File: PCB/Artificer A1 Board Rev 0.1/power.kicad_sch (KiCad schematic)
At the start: 15 parts, among them U12 AXP323, U2 AXP717, U5 CH217K, U6 GT-USB-7010ASV

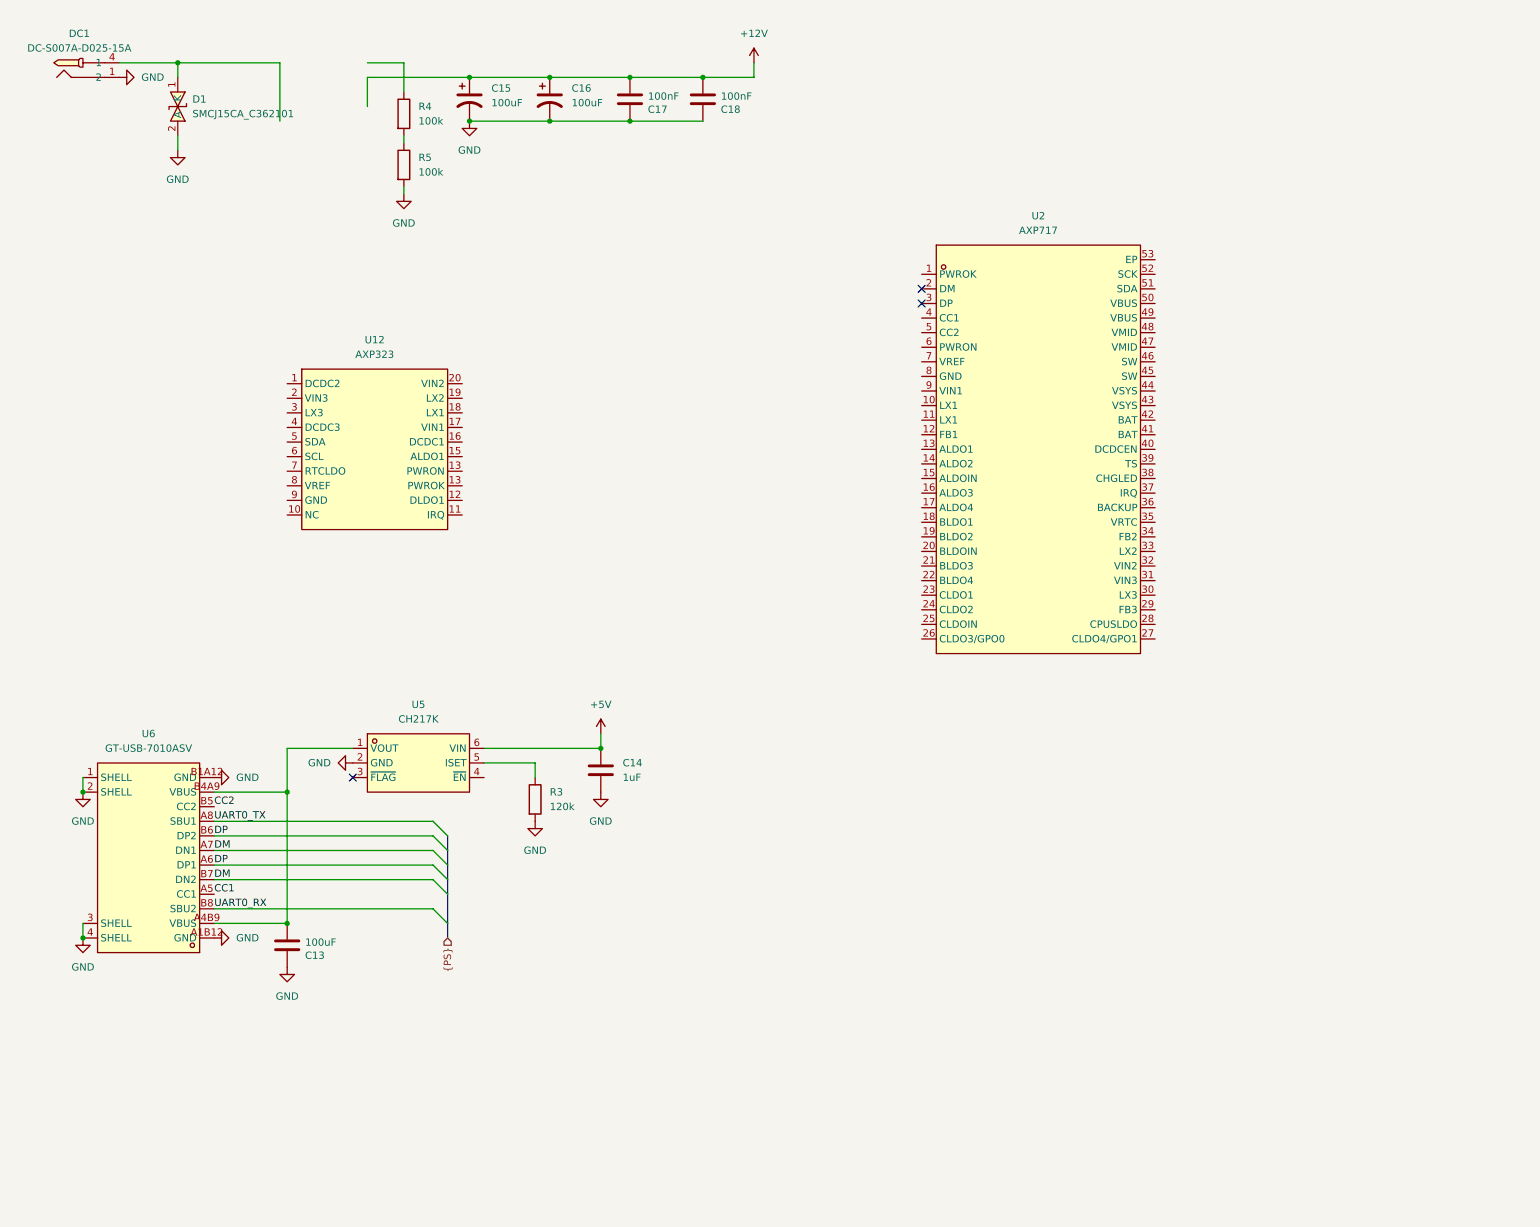
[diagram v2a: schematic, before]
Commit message: dc-dc & started eth PHY
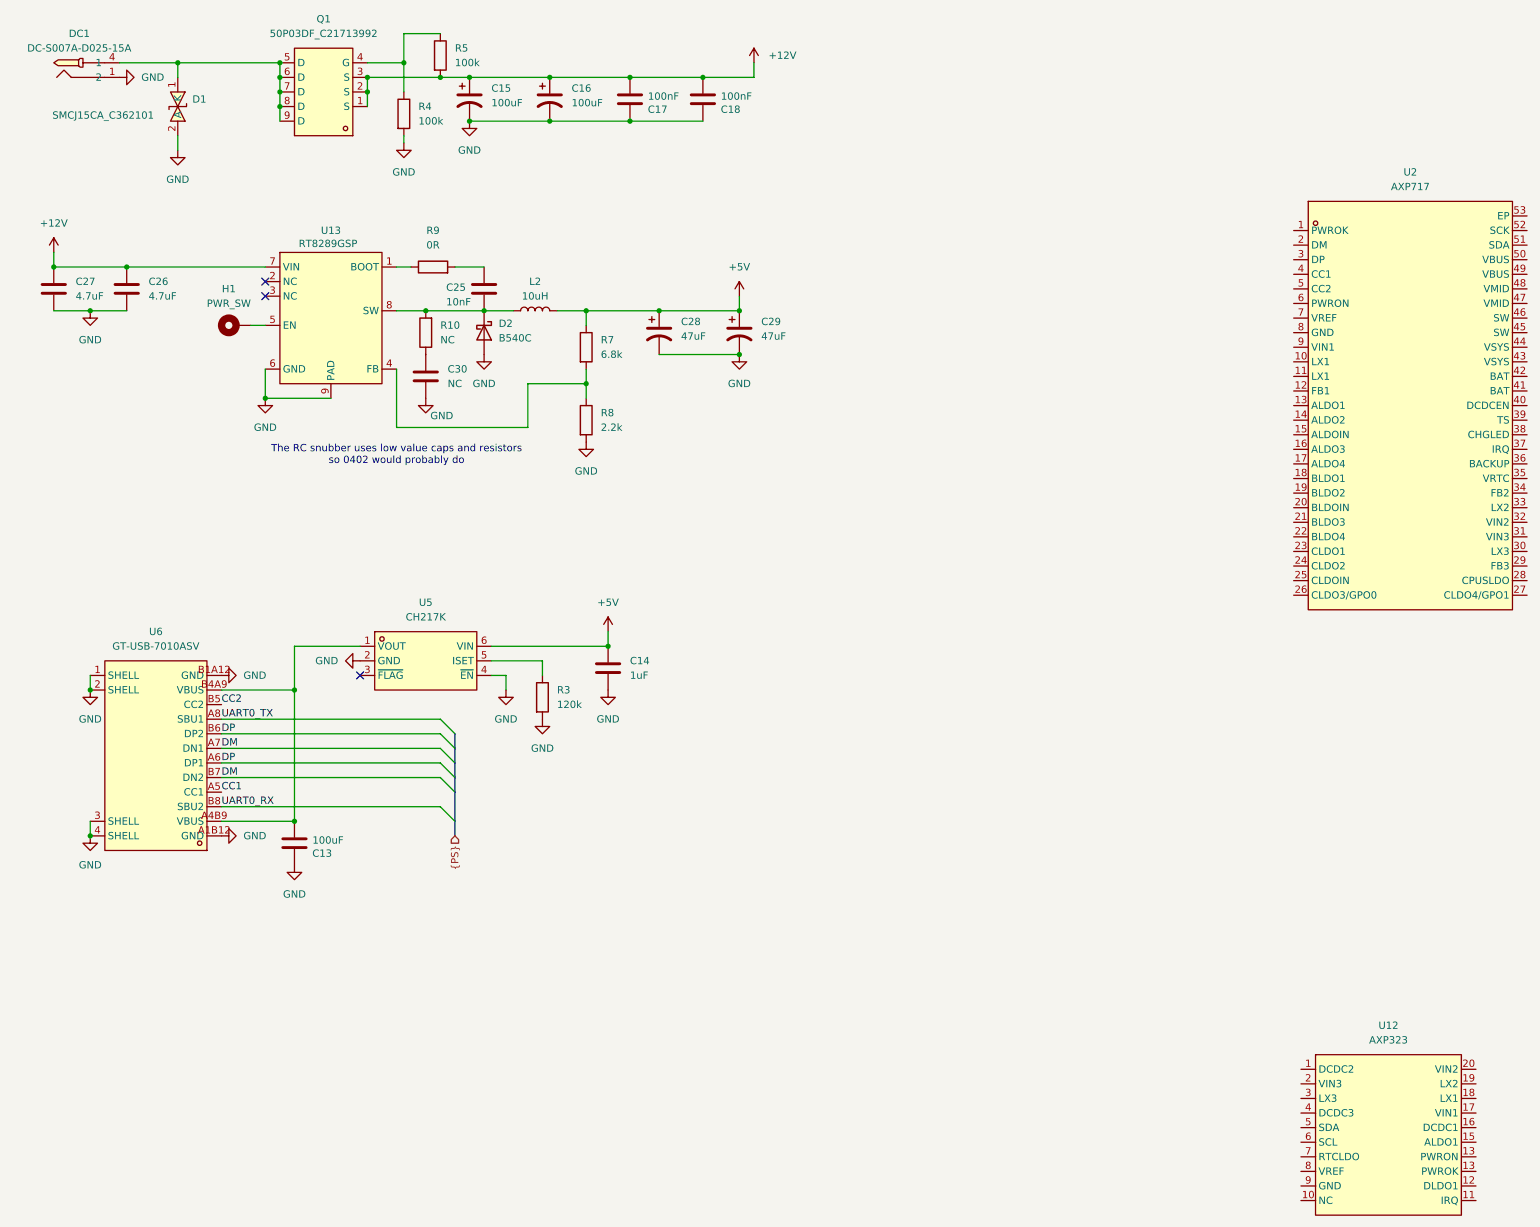
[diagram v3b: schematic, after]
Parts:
- added C25: 10nF, symbol Device:C
- added C26, C27: 4.7uF, symbol Device:C
- added C28, C29: 47uF, symbol Device:C_Polarized_US
- added C30: NC, symbol Device:C
- added D2: B540C, Diode_SMD:D_SMC, symbol Device:D_Schottky
- added H1: PWR_SW, symbol Mechanical:MountingHole_Pad_MP
- added L2: 10uH, symbol Device:L
- added Q1: 50P03DF_C21713992, easyeda:PDFN-8_L3.2-W3.0-P0.65-LS3.3-BL-1, symbol easyeda:30P03D_C20754801
- added R10: NC, symbol Device:R
- added R7: 6.8k, symbol Device:R
- added R8: 2.2k, symbol Device:R
- added R9: 0R, symbol Device:R
- added U13: RT8289GSP, easyeda:SOIC-8_L5.0-W4.0-P1.27-LS6.0-BL-EP2.0, symbol easyeda:RT8289GSP
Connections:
- net +12V: now also R5.2, C26.2, C27.2, Q1.1 (S), Q1.2 (S), Q1.3 (S), U13.7 (VIN)
- net +5V: now also C28.1, C29.1, L2.2, R7.1
- net GND: now also R4.2, U5.4 (~{EN}), C26.1, C27.1, C28.2, C29.2, C30.2, D2.2 (A), R8.2, U13.6 (GND), U13.9 (PAD); no longer R5.2
- net at R5.1: now also R4.1, Q1.4 (G); no longer R4.2
- net at D1.1 (K), DC1.4 (1): now also Q1.5 (D), Q1.6 (D), Q1.7 (D), Q1.8 (D), Q1.9 (D)
- new net: C25.1, D2.1 (K), L2.1, R10.2, U13.8 (SW)
- new net: R9.1, U13.1 (BOOT)
- new net: R7.2, R8.1, U13.4 (FB)
- new net: H1.MP, U13.5 (EN)
- new net: C25.2, R9.2
- new net: C30.1, R10.1
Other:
- note added: "The RC snubber uses low value caps and resistors so 0402 would probably do"
- moved on the sheet: C13, C14, R3, R5, U12, U2, U5, U6

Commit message: added a few accessories
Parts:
- removed C13: 100uF, symbol Device:C
- removed C14: 1uF, symbol Device:C
- removed R3: 120k, symbol Device:R
- removed U5: CH217K, easyeda:SOT-23-6_L2.9-W1.6-P0.95-LS2.8-BL, symbol easyeda:CH217K
- removed U6: GT-USB-7010ASV, easyeda:USB-C-SMD_G-SWITCH_GT-USB-7010ASV, symbol easyeda:GT-USB-7010ASV
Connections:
- no-connect marks 3 -> 2

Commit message: added: sd, wifi, audio, started power, fixed buses
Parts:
- removed H1: PWR_SW, symbol Mechanical:MountingHole_Pad_MP
- removed U12: AXP323, custom footprints:AXP323, symbol AXP323:AXP323
- removed U2: AXP717, easyeda:QFN-52_L6.0-W6.0-P0.40-TL-EP4.7, symbol easyeda:AXP717
- added C100, C101, C102, C103, C104, C105, C106, C107, C87, C95, C96, C97, C98: 2.2uF, symbol Device:C_Small
- added C108, C81, C83, C84, C88, C92, C93, C94, C99: 1uF, symbol Device:C_Small
- added C79, C80: 1nF, symbol Device:C_Small
- added C82, C85, C86, C89, C90, C91: 22uF, symbol Device:C_Small
- added L6, L7, L8: 1uH, symbol Device:L_Small
- added TP10, TP11, TP12, TP13, TP14, TP15, TP16, TP17, TP18, TP19, TP20, TP7, TP9: CPUSLDO, symbol Connector:TestPoint
- added TP3: PWR_SW, symbol Connector:TestPoint
- added TP4: DCDC1, symbol Connector:TestPoint
- added TP5: DCDC2, symbol Connector:TestPoint
- added TP6: DCDC3, symbol Connector:TestPoint
- added TP8: VCC-RTC, symbol Connector:TestPoint
- added U1: T527M00X0DCH, easyeda:BGA-664_L17.0-W17.0_T527, symbol easyeda:T527M00X0DCH
- added U2: AXP323, custom footprints:AXP323, symbol AXP323:AXP323
- added U4: AXP717B, easyeda:QFN-52_L6.0-W6.0-P0.40-TL-EP4.5, symbol easyeda:AXP717B
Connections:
- net +5V: now also C108.1, C81.1, C83.1, C84.1, C94.1, C99.1, U4.15 (ALDOIN), U4.20 (BLDOIN), U4.25 (CLDOIN), U4.31 (VIN3), U4.32 (VIN2), U4.9 (VIN1)
- net GND: now also C100.2, C101.2, C102.2, C103.2, C104.2, C105.2, C106.2, C107.2, C108.2, C79.2, C80.2, C81.2, C82.2, C83.2, C84.2, C85.2, C86.2, C87.2, C88.2, C89.2, C90.2, C91.2, C92.2, C93.2, C94.2, C95.2, C96.2, C97.2, C98.2, C99.2, U1.A1 (GND), U1.A32 (AVSS), U1.A33 (AVSS), U1.AA15 (GND), U1.AA16 (GND), U1.AA18 (GND), U1.AA21 (GND), U1.AA22 (GND), U1.AA26 (GND), U1.AA30 (GND), U1.AA32 (GND), U1.AB10 (GND), U1.AB11 (GND), U1.AB12 (GND), U1.AB14 (GND), U1.AB15 (GND), U1.AB17 (GND), U1.AC1 (GND), U1.AC26 (GND), U1.AC29 (GND), U1.AC33 (GND), U1.AD11 (GND), U1.AD13 (GND), U1.AD14 (GND), U1.AD20 (GND), U1.AD21 (GND), U1.AD22 (GND), U1.AD9 (GND), U1.AE12 (GND), U1.AE14 (GND), U1.AE18 (GND), U1.AE19 (GND), U1.AE20 (GND), U1.AE21 (GND), U1.AE22 (GND), U1.AE23 (GND), U1.AE24 (GND), U1.AE25 (GND), U1.AE26 (GND), U1.AE29 (GND), U1.AE32 (GND), U1.AE9 (GND), U1.AG11 (GND), U1.AG25 (GND), U1.AG28 (GND), U1.AG3 (GND), U1.AG31 (GND), U1.AG33 (GND), U1.AG6 (GND), U1.AG7 (GND), U1.AH27 (GND), U1.AH32 (GND), U1.AH7 (GND), U1.AH9 (GND), U1.AJ13 (GND), U1.AJ19 (GND), U1.AJ21 (GND), U1.AJ23 (GND), U1.AK11 (GND), U1.AK32 (GND), U1.AK5 (GND), U1.AL12 (GND), U1.AL13 (GND), U1.AL14 (GND), U1.AL3 (GND), U1.AL9 (GND), U1.AM20 (GND), U1.AM26 (GND), U1.AM29 (GND), U1.AM5 (GND), U1.AN1 (GND), U1.AN10 (GND), U1.AN11 (GND), U1.AN18 (GND), U1.AN22 (GND), U1.AN24 (GND), U1.AN28 (GND), U1.AN31 (GND), U1.AN33 (GND), U1.C10 (GND), U1.C12 (GND), U1.C14 (GND), U1.C18 (GND), U1.C20 (GND), U1.C22 (AVSS), U1.C24 (AVSS), U1.C26 (AVSS), U1.C28 (AVSS), U1.C30 (AVSS), U1.C31 (AVSS), U1.C6 (GND), U1.C8 (GND), U1.D6 (GND), U1.E29 (AVSS), U1.E3 (GND), U1.F10 (GND), U1.F12 (GND), U1.F22 (AVSS), U1.F24 (AVSS), U1.F6 (GND), U1.F8 (GND), U1.G10 (GND), U1.G14 (GND), U1.G18 (GND), U1.G26 (AVSS), U1.G28 (AVSS), U1.G29 (GND), U1.G3 (GND), U1.G8 (GND), U1.H24 (AVSS), U1.J10 (GND), U1.J12 (GND), U1.J13 (GND), U1.J17 (AVSS), U1.J21 (AVSS), U1.J22 (AVSS), U1.J23 (AVSS), U1.J26 (AVSS), U1.J28 (GND), U1.J3 (GND), U1.J31 (GND), U1.J6 (GND), U1.J9 (GND), U1.K10 (GND), U1.K11 (GND), U1.K12 (GND), U1.K15 (AVSS), U1.K16 (AVSS), U1.K21 (AVSS), U1.K22 (AVSS), U1.K24 (AVSS), U1.K25 (AVSS), U1.K26 (GND), U1.K9 (GND), U1.L10 (GND), U1.L12 (GND), U1.L13 (GND), U1.L16 (AVSS), U1.L19 (AVSS), U1.L24 (AVSS), U1.L27 (GND), U1.L3 (GND), U1.L30 (GND), U1.L33 (GND), U1.L6 (GND), U1.M13 (GND), U1.M16 (AVSS), U1.M18 (AVSS), U1.M19 (AVSS), U1.N10 (GND), U1.N12 (GND), U1.N15 (GND), U1.N18 (GND), U1.N19 (GND), U1.N22 (GND), U1.N26 (GND), U1.N27 (GND), U1.N3 (GND), U1.N30 (GND), U1.N6 (GND), U1.P11 (GND), U1.P16 (GND), U1.P19 (GND), U1.P24 (GND), U1.R11 (GND), U1.R13 (GND), U1.R19 (GND), U1.R24 (GND), U1.R27 (GND), U1.R3 (GND), U1.R7 (GND), U1.T15 (GND), U1.T16 (GND), U1.T18 (GND), U1.T24 (GND), U1.U14 (GND), U1.U16 (GND), U1.U25 (GND), U1.U27 (GND), U1.U7 (GND), U1.V18 (GND), U1.V19 (GND), U1.W12 (GND), U1.W13 (GND), U1.W15 (GND), U1.W16 (GND), U1.W22 (GND), U1.W27 (GND), U1.W30 (GND), U1.Y15 (GND), U1.Y18 (GND), U1.Y22 (GND), U1.Y23 (GND), U1.Y26 (GND), U2.21 (EPAD), U2.9 (GND), U4.53 (EP), U4.8 (GND)
- net at U13.5 (EN): now also TP3.1
- new net: L6.1, U4.10 (LX1_1), U4.11 (LX1_2)
- new net: L8.1, U4.30 (LX3)
- new net: L7.1, U4.33 (LX2)
- new net: C88.1, U4.7 (VREF)
- new net: U1.AA12 (VDDDNR), U1.AA13 (VDDDNR), U1.Y12 (VDDDNR), U1.Y13 (VDDDNR)
- new net: U1.N21 (VDDDE), U1.P21 (VDDDE)
- new net: U1.T11 (VDDGPU), U1.T13 (VDDGPU), U1.U12 (VDDGPU), U1.U13 (VDDGPU)
- new net: U1.T19 (VDDCPUB), U1.T21 (VDDCPUB), U1.T22 (VDDCPUB), U1.U18 (VDDCPUB), U1.U19 (VDDCPUB), U1.U21 (VDDCPUB), U1.U22 (VDDCPUB)
- new net: U1.W19 (VDDCPUL), U1.W21 (VDDCPUL), U1.Y19 (VDDCPUL), U1.Y21 (VDDCPUL)
- new net ALDO1: C104.1, TP17.1, U4.13 (ALDO1)
- new net ALDO2: C105.1, TP18.1, U4.14 (ALDO2)
- new net ALDO3: C106.1, TP19.1, U4.16 (ALDO3)
- new net ALDO4: C107.1, TP20.1, U4.17 (ALDO4)
- new net AP-NMI: C79.1, U4.37 (IRQ)
- new net AP-RESET: C80.1, U4.1 (PWROK)
- new net BLDO1: C100.1, TP16.1, U4.18 (BLDO1)
- new net BLDO2: C101.1, TP15.1, U4.19 (BLDO2)
- new net BLDO3: C102.1, TP14.1, U4.21 (BLDO3)
- new net BLDO4: C103.1, TP13.1, U4.22 (BLDO4)
- new net CLDO1: C95.1, TP9.1, U4.23 (CLDO1)
- new net CLDO2: C96.1, TP10.1, U4.24 (CLDO2)
- new net CLDO3: C97.1, TP11.1, U4.26 (CLDO3/GPO0)
- new net CLDO4: C98.1, TP12.1, U4.27 (CLDO4/GPO1)
- new net CPUSLDO: C87.1, TP7.1, U4.28 (CPUSLDO)
- new net DCDC1: C82.1, C89.1, L6.2, TP4.1
- new net DCDC2: C85.1, C90.1, L7.2, TP5.1
- new net DCDC3: C86.1, C91.1, L8.2, TP6.1, U4.29 (FB3)
- new net PMU-SCK: U4.52 (SCK)
- new net PMU-SDA: U4.51 (SDA)
- new net VCC-RTC: C92.1, TP8.1, U4.35 (VRTC)
- new net VCC-RTC-IN: C93.1, U4.36 (BACKUP)
- new net VDD06-DRAM: U1.AC17 (VCCDRAML), U1.AC18 (VCCDRAML), U1.AC19 (VCCDRAML), U1.AC20 (VCCDRAML), U1.AC22 (VCCDRAML)
- new net VDD11-DRAM: U1.AA24 (VCCDRAM), U1.AB24 (VCCDRAM), U1.AC24 (VCCDRAM), U1.W23 (VCCDRAM), U1.W24 (VCCDRAM), U1.W25 (VCCDRAM), U1.Y24 (VCCDRAM)
- new net VDD18-DRAM: U1.AD25 (VDD18-DRAM)
- no-connect marks 2 -> 8
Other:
- note added: "VDD-CPULFB"
- note added: "VDD-SYSFB"

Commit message: added features
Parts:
- added C109, C110, C111, C113: 22uF, symbol Device:C_Small
- added C112, C118, C119, C120: 4.7uF, symbol Device:C_Small
- added C114, C115, C116, C117, C121, C122, C124, C125, C126, C127: 10uF, symbol Device:C_Small
- added C123: 100nF, symbol Device:C_Small
- added C128: 1uF, symbol Device:C_Small
- added C129, C130, C131: 2.2uF, symbol Device:C_Small
- added C132, C133: 4.7uF, symbol Device:C
- added C134: NC, symbol Device:C
- added C135: 10nF, symbol Device:C
- added C136, C137: 47uF, symbol Device:C_Polarized_US
- added D13: B540C, Diode_SMD:D_SMC, symbol Device:D_Schottky
- added D14, D15: SS54, Diode_SMD:D_SMA, symbol Device:D_Schottky
- added L10, L11, L12, L9: 1uH, symbol Device:L_Small
- added L13: 10uH, symbol Device:L
- added NT1, NT10, NT11, NT12, NT13, NT14, NT15, NT16, NT17, NT18, NT19, NT2, NT20, NT21, NT22, NT23, NT24, NT25, NT26, NT27, NT28, NT29, NT3, NT30, NT31, NT32, NT33, NT34, NT35, NT36, NT37, NT38, NT39, NT4, NT40, NT41, NT42, NT43, NT44, NT45, NT46, NT47, NT48, NT49, NT5, NT50, NT51, NT52, NT53, NT54, NT6, NT7, NT8, NT9: NetTie_2, symbol Device:NetTie_2
- added PS: CPUSLDO, symbol Connector:TestPoint
- added R77, R80: 0R, symbol Device:R_Small
- added R78: NC, symbol Device:R_Small
- added R79: 10k, symbol Device:R_Small
- added R81: NC, symbol Device:R
- added R82: 0R, symbol Device:R
- added R83: 56k, symbol Device:R
- added R84: 33k, symbol Device:R
- added TP21, TP22: DCDC1, symbol Connector:TestPoint
- added TP23: 3V3_PCIE_PWR_SW, symbol Connector:TestPoint
- added U15: RT8289GSP, easyeda:SOIC-8_L5.0-W4.0-P1.27-LS6.0-BL-EP2.0, symbol easyeda:RT8289GSP
- added U16: ETA8121S2G, easyeda:SOT-23-6_L2.9-W1.6-P0.95-LS2.9-BL, symbol easyeda:ETA8121S2G
- Q1: LCSC Part C21713992 -> C20754801
- R7: value 6.8k -> 68k
- R8: value 2.2k -> 22k
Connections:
- net +12V: now also C132.2, C133.2, U15.7 (VIN)
- net +5V: no longer C28.1, C29.1, L2.2, R7.1
- net ALDO1: now also NT12.1
- net ALDO2: now also NT13.1
- net ALDO3: now also NT14.1, NT15.1
- net ALDO4: now also NT16.1, NT17.1, NT18.1, NT19.1, NT20.1
- net AP-RESET: now also R80.1
- net BLDO1: now also NT21.1, NT22.1
- net BLDO2: now also C123.1, NT23.1, NT24.1, R79.1
- net BLDO3: now also NT25.1
- net BLDO4: now also NT26.1
- net CLDO1: now also NT28.1, NT29.1, NT30.1, NT31.1, NT32.1, NT33.1, NT34.1, NT35.1, NT36.1, NT37.1, NT38.1
- net CLDO2: now also NT27.1
- net CLDO3: now also NT43.1
- net CLDO4: now also NT40.1, NT41.1
- net CPUSLDO: now also NT1.1
- net DCDC1: now also NT3.1
- net DCDC2: now also NT10.1, NT2.1, NT4.1, NT5.1, NT6.1, NT7.1, NT8.1, NT9.1
- net DCDC3: now also NT11.1
- net GND: now also C109.2, C110.2, C111.2, C112.1, C113.2, C114.2, C115.2, C116.2, C117.2, C118.1, C119.1, C120.1, C121.2, C122.2, C123.2, C124.2, C125.2, C126.2, C127.2, C128.1, C129.2, C130.2, C131.2, C132.1, C133.1, C134.2, C136.2, C137.2, D13.2 (A), R78.1, R84.2, U15.6 (GND), U15.9 (PAD)
- net PMU-SCK: now also U2.5 (SDA), TP21.1
- net PMU-SDA: now also U2.6 (SCL), TP22.1
- net VDD18-DRAM: now also NT18.2; no longer U1.AD25 (VDD18-DRAM)
- net 323-DLDO1: now reaches U2.12 (DLDO1)
- net 323-DLDO1: now also C130.1
- net at U2.13 (PWROK): now also R80.2
- net at U2.14 (PWRON): now also R79.2
- net 323-ALDO1: now reaches U2.15 (ALDO1)
- net 323-ALDO1: now also C129.1
- net PS: now reaches U2.17 (VIN1)
- net PS: now also U2.2 (VIN3), U2.20 (VIN2), U4.43 (VSYS_1), U4.44 (VSYS_2), U4.47 (VMID_1), U4.48 (VMID_2), C113.1, C114.1, C115.1, C118.2, C119.2, C120.2, PS.1
- net at U2.18 (LX1): now also L10.1
- net at U2.19 (LX2): now also L11.1
- net at U2.3 (LX3): now also L12.1
- net 323-RTCLDO: now reaches U2.7 (RTCLDO)
- net 323-RTCLDO: now also C131.1
- net at U2.8 (VREF): now also C128.2
- net at U4.38 (FB4): now also R77.2
- net at U4.39 (TS): now also R78.2
- net VBAT: now reaches U4.41 (BAT_1)
- net VBAT: now also U4.42 (BAT_2), C112.2
- net at U4.45 (SW_1): now also U4.46 (SW_2), L9.2
- net 5V_SYS: now reaches U4.49 (VBUS_1)
- net 5V_SYS: now also U4.50 (VBUS_2), C116.1, C117.1, D14.1 (K), NT39.2
- removed net VDD06-DRAM: U1.AC17 (VCCDRAML), U1.AC18 (VCCDRAML), U1.AC19 (VCCDRAML), U1.AC20 (VCCDRAML), U1.AC22 (VCCDRAML)
- removed net VDD11-DRAM: U1.AA24 (VCCDRAM), U1.AB24 (VCCDRAM), U1.AC24 (VCCDRAM), U1.W23 (VCCDRAM), U1.W24 (VCCDRAM), U1.W25 (VCCDRAM), U1.Y24 (VCCDRAM)
- new net: C136.1, C137.1, D15.2 (A), L13.2, R83.1
- new net: C28.1, C29.1, D14.2 (A), L2.2, R7.1
- new net: C135.1, D13.1 (K), L13.1, R81.2, U15.8 (SW)
- new net: C135.2, R82.2
- new net: C134.1, R81.1
- new net: R83.2, R84.1, U15.4 (FB)
- new net: R82.1, U15.1 (BOOT)
- new net: TP23.1, U15.5 (EN)
- new net 323-DCDC1/2: C121.1, C122.1, C124.1, C125.1, L10.2, L11.2, NT44.1
- new net 323-DCDC3: C126.1, C127.1, L12.2, NT45.1
- new net AFVCC-CSI: NT25.2
- new net AVCC: NT16.2
- new net AVDD-CSI: NT12.2
- new net CPVIN: NT28.2
- new net DCDC4: C109.1, C110.1, C111.1, L9.1, NT42.1, NT46.1, NT47.1, NT48.1, NT49.1, NT50.1, NT51.1, NT52.1, NT53.1, NT54.1, R77.1
- new net DVDD-CSI: NT26.2
- new net PCIE_3V3: D15.1 (K)
- new net VBUS: NT39.1
- new net VCC-3V3: NT54.2
- new net VCC-ADC: NT20.2
- new net VCC-DCXO: NT19.2
- new net VCC-EFUSE: NT33.2
- new net VCC-GMAC: NT50.2
- new net VCC-LCD: NT40.2
- new net VCC-LVDS0: NT30.2
- new net VCC-LVDS1: NT37.2
- new net VCC-MCSI: NT31.2
- new net VCC-PC: NT29.2
- new net VCC-PD: NT49.2
- new net VCC-PE: NT47.2
- new net VCC-PG: NT21.2
- new net VCC-PI: NT51.2
- new net VCC-PJ: NT38.2
- new net VCC-PK: NT48.2
- new net VCC-PL: NT14.2
- new net VCC-PLL: NT17.2
- new net VCC-PM: NT23.2
- new net VCC-WIFI: NT53.2
- new net VCC18-EDP: NT35.2
- new net VCC18-HDMI: NT36.2
- new net VCC18-PCIE: NT34.2
- new net VCC33-USB: NT15.2, NT52.2
- new net VCC3V3-CSI: NT27.2, NT43.2
- new net VCC3V3_PHY1: NT41.2
- new net VCCIO-WIFI: NT22.2
- new net VDD-CPUB: NT44.2
- new net VDD-CPUL: NT3.2
- new net VDD-CPUS: NT1.2
- new net VDD-DE: NT7.2
- new net VDD-DNR: NT45.2
- new net VDD-DRAM: NT11.2, NT42.2
- new net VDD-GPU: NT5.2
- new net VDD-SYS: NT4.2
- new net VDD-VE: NT6.2
- new net VDD09-EDP: NT9.2
- new net VDD09-HDMI: NT10.2, NT46.2
- new net VDD09-PCIE: NT8.2
- new net VDD09-USB: NT2.2
- new net VDD18-LPDDR: NT24.2
- no-connect marks 8 -> 13
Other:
- note added: "0.9V"
- note added: "1.8V"
- note added: "3.3V"
- note added: "5 Amp"
- note added: "C0402_BGA"
- note added: "C0603"
- note added: "Connect to RTC power input on SoC"
- note added: "This DCDC can supply 5A. PCIE allows for 3Amp of current to be drawn on the 3.3V rail."
- note added: "VDD-CPUBFB"
- note added: "VDD-DNRFB"
- moved on the sheet: C79, C80
